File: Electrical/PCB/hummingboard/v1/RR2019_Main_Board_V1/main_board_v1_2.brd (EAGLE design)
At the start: 100 x 75 mm, 143 parts, among them CN1 MIRCO_B, IC1 OR_SC70-5, J10 I2C_5V_4, J11 SERVO_LEFT, J12 SERVO_RIGHT, J13 ESC, J14 5V_INPUT, J15 QUAD_ENCODER_2, J16 7.2V_INPUT, J17 I2C_5V_FXIO_1, J18 I2C_5V_FXIO_2, J19 JETSON_TRIGGER, J2 REAR_ENCODER, J20 QUAD_ENCODER_1, J21 BLDC_HALL, J22 SPI_FXIO_1, J3 FRONT_ENCODER, J4 I2C_1V8_1, J5 SPI_2, J6 WIRELESS_MODULE, J7 UART_0, J8 UART_2, J9 STEERING_ANGLE, Q1 BSS138, Q3 DMP2066LSN, Q4 BSS138, Q5 BSS138, Q6 BSS138, Q7 BSS138, Q8 BSS138, U3 ICM-20948, U4 PCA9306

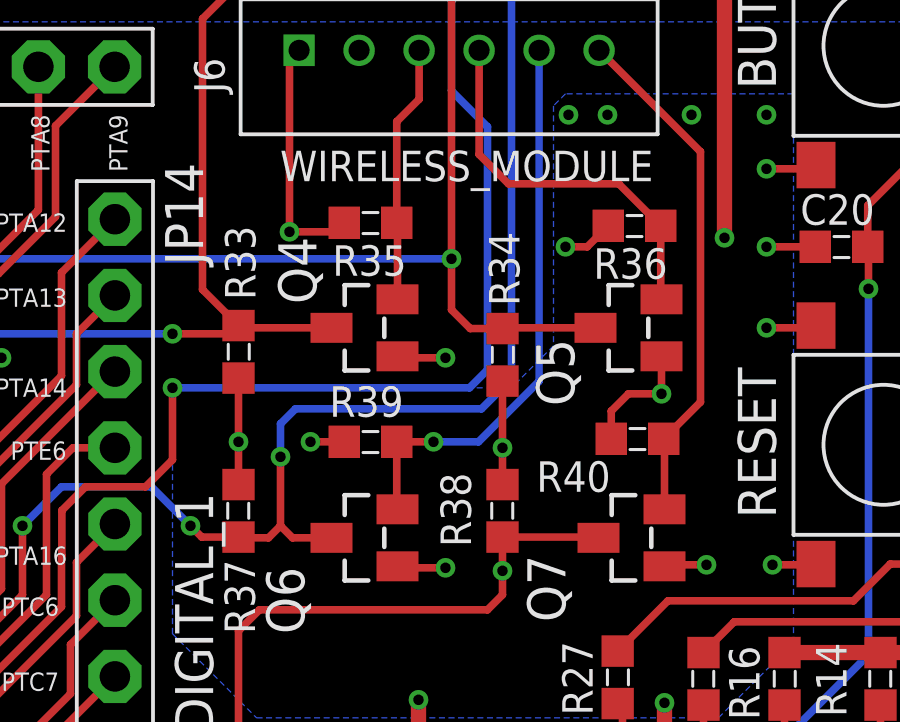
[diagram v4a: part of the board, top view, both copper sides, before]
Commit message: fix the MOSI/MISO direction
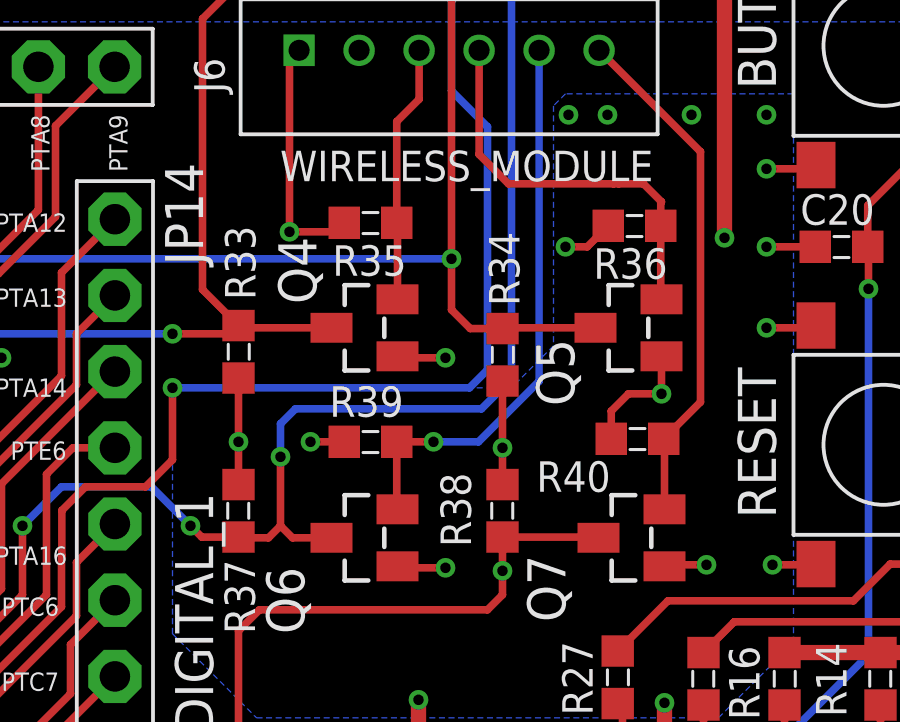
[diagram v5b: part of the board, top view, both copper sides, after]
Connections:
- net 3V3_SPI0_MISO: now also J6.4, Q5.2, R36.1; no longer J6.5, Q6.2, R39.1
- net 3V3_SPI0_MOSI: now also J6.5, Q6.2, R39.1; no longer J6.4, Q5.2, R36.1
- net SPI0_MISO: now also J5.4, Q5.3, R34.1, U$1.93; no longer J5.5, Q6.3, R37.1, U$1.85
- net SPI0_MOSI: now also J5.5, Q6.3, R37.1, U$1.85; no longer J5.4, Q5.3, R34.1, U$1.93
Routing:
- net 3V3_SPI0_MOSI: track 13.0 -> 18.9 mm, vias 0 -> 1
- net 3V3_SPI0_MISO: track 18.9 -> 13.5 mm, vias 1 -> 0
- net SPI0_MISO: track 54.9 -> 56.2 mm, vias 3 -> 2
- net SPI0_MOSI: track 56.2 -> 54.9 mm, vias 2 -> 3
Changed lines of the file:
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@@
 <layer number="13" name="Route13" color="21" fill="1" visible="no" active="no"/>
 <layer number="14" name="Route14" color="22" fill="1" visible="no" active="no"/>
-<layer number="15" name="POWER" color="23" fill="6" visible="no" active="yes"/>
-<layer number="16" name="Bottom" color="1" fill="1" visible="no" active="yes"/>
-<layer number="17" name="Pads" color="2" fill="1" visible="no" active="yes"/>
+<layer number="15" name="POWER" color="23" fill="6" visible="yes" active="yes"/>
+<layer number="16" name="Bottom" color="1" fill="1" visible="yes" active="yes"/>
+<layer number="17" name="Pads" color="2" fill="1" visible="yes" active="yes"/>
 <layer number="18" name="Vias" color="2" fill="1" visible="yes" active="yes"/>
 <layer number="19" name="Unrouted" color="6" fill="1" visible="yes" active="yes"/>
@@
 </signal>
 <signal name="SPI0_MISO">
+<contactref element="U$1" pad="93"/>
+<contactref element="Q5" pad="3"/>
+<contactref element="R34" pad="1"/>
+<wire x1="62" y1="55.875" x2="62.025" y2="55.9" width="0.254" layer="1"/>
+<wire x1="62.025" y1="55.9" x2="65.1" y2="55.9" width="0.254" layer="1"/>
+<contactref element="J5" pad="4"/>
+<wire x1="60.3" y1="71.21" x2="61.24" y2="72.15" width="0.254" layer="1"/>
+<wire x1="34.85" y1="47.55" x2="33.3" y2="49.1" width="0.254" layer="1"/>
+<via x="33.3" y="49.1" extent="1-16" drill="0.35"/>
+<wire x1="33.3" y1="49.1" x2="33.3" y2="49.5" width="0.254" layer="16"/>
+<wire x1="33.3" y1="49.5" x2="42" y2="58.2" width="0.254" layer="16"/>
+<wire x1="42" y1="58.2" x2="60.3" y2="58.2" width="0.254" layer="16"/>
+<via x="60.3" y="58.2" extent="1-16" drill="0.35"/>
+<wire x1="60.3" y1="58.2" x2="60.3" y2="71.21" width="0.254" layer="1"/>
+<wire x1="60.3" y1="58.2" x2="60.3" y2="56.5" width="0.254" layer="1"/>
+<wire x1="60.3" y1="56.5" x2="60.925" y2="55.875" width="0.254" layer="1"/>
+<wire x1="60.925" y1="55.875" x2="62" y2="55.875" width="0.254" layer="1"/>
+<wire x1="36.755" y1="47.55" x2="34.85" y2="47.55" width="0.254" layer="1"/>
+</signal>
+<signal name="SPI0_MOSI">
 <contactref element="U$1" pad="85"/>
 <contactref element="R37" pad="1"/>
 <contactref element="Q6" pad="3"/>
-<contactref element="J5" pad="5"/>
-<wire x1="56.275" y1="48.925" x2="56.3" y2="48.9" width="0.254" layer="1"/>
 <via x="46" y="49.3" extent="1-16" drill="0.35"/>
 <wire x1="53.2" y1="48.925" x2="51.975" y2="48.925" width="0.254" layer="1"/>
@@
 <wire x1="50.3" y1="50.6" x2="51.6" y2="49.3" width="0.254" layer="16"/>
 <wire x1="47.3" y1="50.6" x2="50.3" y2="50.6" width="0.254" layer="16"/>
-<wire x1="36.755" y1="43.55" x2="42.55" y2="43.55" width="0.254" layer="1"/>
 <wire x1="42.55" y1="43.55" x2="46" y2="47" width="0.254" layer="1"/>
 <wire x1="46" y1="47" x2="46" y2="49.3" width="0.254" layer="1"/>
+<contactref element="J5" pad="5"/>
 <wire x1="63.24" y1="72.15" x2="62.3" y2="71.21" width="0.254" layer="16"/>
 <wire x1="54.6" y1="52.7" x2="55.1" y2="53.2" width="0.254" layer="16"/>
@@
 <wire x1="61.3" y1="53.2" x2="55.1" y2="53.2" width="0.254" layer="16"/>
 <via x="54.6" y="51.6" extent="1-16" drill="0.35"/>
-<wire x1="53.225" y1="48.9" x2="53.2" y2="48.925" width="0.254" layer="1"/>
 <wire x1="56.25" y1="48.9" x2="56.275" y2="48.925" width="0.254" layer="1"/>
 <wire x1="54.6" y1="51.6" x2="54.6" y2="52.7" width="0.254" layer="16"/>
 <wire x1="54.6" y1="51.6" x2="54.6" y2="49.3" width="0.254" layer="1"/>
-<wire x1="54.2" y1="48.9" x2="53.225" y2="48.9" width="0.254" layer="1"/>
-<wire x1="54.6" y1="49.3" x2="54.2" y2="48.9" width="0.254" layer="1"/>
+<wire x1="54.2" y1="48.9" x2="54.6" y2="49.3" width="0.254" layer="1"/>
 <wire x1="54.6" y1="49.3" x2="55" y2="48.9" width="0.254" layer="1"/>
-<wire x1="55" y1="48.9" x2="56.25" y2="48.9" width="0.254" layer="1"/>
-</signal>
-<signal name="SPI0_MOSI">
-<contactref element="U$1" pad="93"/>
-<contactref element="Q5" pad="3"/>
-<contactref element="R34" pad="1"/>
-<contactref element="J5" pad="4"/>
-<wire x1="60.3" y1="71.21" x2="61.24" y2="72.15" width="0.254" layer="1"/>
-<wire x1="36.755" y1="47.55" x2="34.85" y2="47.55" width="0.254" layer="1"/>
-<wire x1="34.85" y1="47.55" x2="33.3" y2="49.1" width="0.254" layer="1"/>
-<via x="33.3" y="49.1" extent="1-16" drill="0.35"/>
-<wire x1="33.3" y1="49.1" x2="33.3" y2="49.5" width="0.254" layer="16"/>
-<wire x1="33.3" y1="49.5" x2="42" y2="58.2" width="0.254" layer="16"/>
-<wire x1="42" y1="58.2" x2="60.3" y2="58.2" width="0.254" layer="16"/>
-<via x="60.3" y="58.2" extent="1-16" drill="0.35"/>
-<wire x1="60.3" y1="58.2" x2="60.3" y2="71.21" width="0.254" layer="1"/>
-<wire x1="60.925" y1="55.875" x2="62" y2="55.875" width="0.254" layer="1"/>
-<wire x1="60.3" y1="58.2" x2="60.3" y2="56.5" width="0.254" layer="1"/>
-<wire x1="60.3" y1="56.5" x2="60.925" y2="55.875" width="0.254" layer="1"/>
-<wire x1="62" y1="55.875" x2="62.025" y2="55.9" width="0.254" layer="1"/>
-<wire x1="62.025" y1="55.9" x2="65.1" y2="55.9" width="0.254" layer="1"/>
+<wire x1="36.755" y1="43.55" x2="42.55" y2="43.55" width="0.254" layer="1"/>
+<wire x1="53.2" y1="48.925" x2="53.225" y2="48.9" width="0.254" layer="1"/>
+<wire x1="53.225" y1="48.9" x2="54.2" y2="48.9" width="0.254" layer="1"/>
+<wire x1="55" y1="48.9" x2="56.3" y2="48.9" width="0.254" layer="1"/>
+<wire x1="56.3" y1="48.9" x2="56.25" y2="48.9" width="0" layer="19" extent="1-1"/>
 </signal>
 <signal name="SPI0_SCK">
@@
 </signal>
 <signal name="3V3_SPI0_MOSI">
-<contactref element="Q5" pad="2"/>
-<contactref element="R36" pad="1"/>
-<contactref element="J6" pad="4"/>
-<wire x1="67.3" y1="56.85" x2="67.275" y2="56.875" width="0.254" layer="1"/>
-<wire x1="67.275" y1="56.875" x2="67.275" y2="59.3" width="0.254" layer="1"/>
-<wire x1="67.275" y1="59.3" x2="65.875" y2="60.7" width="0.254" layer="1"/>
-<wire x1="65.875" y1="60.7" x2="62.2" y2="60.7" width="0.254" layer="1"/>
-<wire x1="62.2" y1="60.7" x2="61.22" y2="61.68" width="0.254" layer="1"/>
-<wire x1="61.22" y1="61.68" x2="61.22" y2="65.15" width="0.254" layer="1"/>
-</signal>
-<signal name="3V3_SPI0_MISO">
 <contactref element="Q6" pad="2"/>
 <contactref element="R39" pad="1"/>
-<contactref element="J6" pad="5"/>
 <wire x1="58.475" y1="52.1" x2="58.475" y2="49.875" width="0.254" layer="1"/>
 <wire x1="58.475" y1="49.875" x2="58.5" y2="49.85" width="0.254" layer="1"/>
+<contactref element="J6" pad="5"/>
 <wire x1="63.22" y1="65.15" x2="63.22" y2="54.12" width="0.254" layer="16"/>
 <wire x1="63.22" y1="54.12" x2="61.2" y2="52.1" width="0.254" layer="16"/>
 <wire x1="61.2" y1="52.1" x2="59.7" y2="52.1" width="0.254" layer="16"/>
 <via x="59.7" y="52.1" extent="1-16" drill="0.35"/>
-<wire x1="59.7" y1="52.1" x2="58.475" y2="52.1" width="0.254" layer="1"/>
+<wire x1="58.475" y1="52.1" x2="59.7" y2="52.1" width="0.254" layer="1"/>
+</signal>
+<signal name="3V3_SPI0_MISO">
+<contactref element="Q5" pad="2"/>
+<contactref element="R36" pad="1"/>
+<wire x1="67.3" y1="56.85" x2="67.275" y2="56.875" width="0.254" layer="1"/>
+<wire x1="67.275" y1="56.875" x2="67.275" y2="59.3" width="0.254" layer="1"/>
+<contactref element="J6" pad="4"/>
+<wire x1="65.875" y1="60.7" x2="65.7" y2="60.7" width="0.254" layer="1"/>
+<wire x1="65.7" y1="60.7" x2="62.2" y2="60.7" width="0.254" layer="1"/>
+<wire x1="62.2" y1="60.7" x2="61.22" y2="61.68" width="0.254" layer="1"/>
+<wire x1="61.22" y1="61.68" x2="61.22" y2="65.15" width="0.254" layer="1"/>
+<wire x1="65.875" y1="60.7" x2="66.7" y2="60.7" width="0.254" layer="1"/>
+<wire x1="66.7" y1="60.7" x2="67.3" y2="60.1" width="0.254" layer="1"/>
+<wire x1="67.3" y1="60.1" x2="67.275" y2="60.075" width="0.254" layer="1"/>
+<wire x1="67.275" y1="60.075" x2="67.275" y2="59.3" width="0.254" layer="1"/>
 </signal>
 <signal name="3V3_SPI0_PCS0">
